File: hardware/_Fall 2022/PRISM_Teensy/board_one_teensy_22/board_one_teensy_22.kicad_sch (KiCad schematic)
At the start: 14 parts, among them J1 EAST, J2 CORE_IO, J3 USB_micro, U1 Teensy4.1, U2 BNO055_Breakout, U3 3966

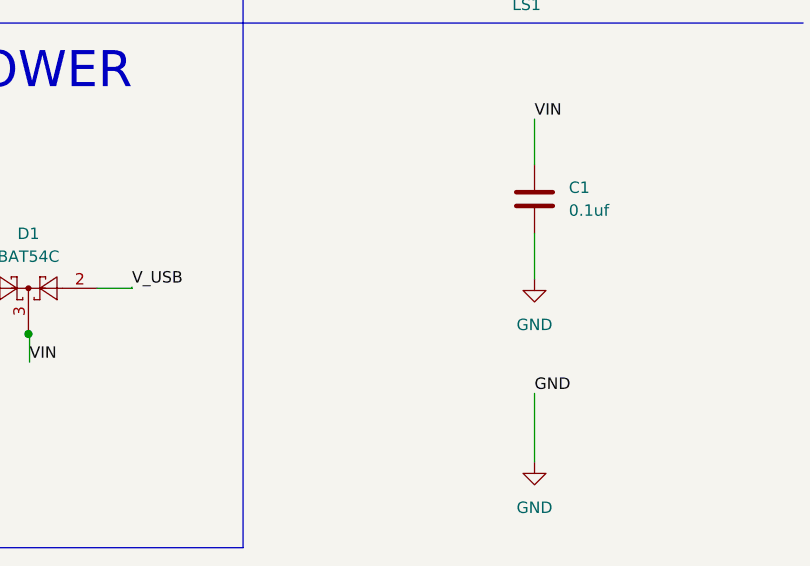
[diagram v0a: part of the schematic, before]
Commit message: Board one changed resistor size
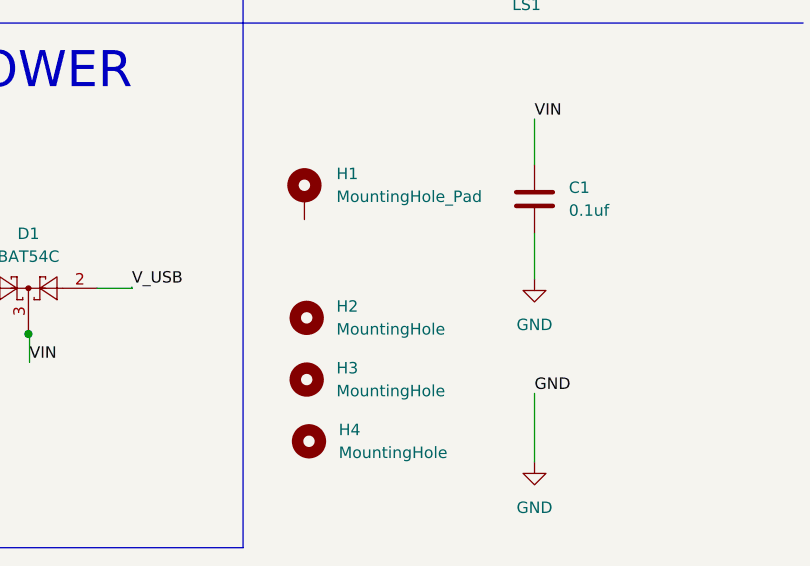
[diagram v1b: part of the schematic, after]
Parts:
- added H1: MountingHole_Pad, MountingHole:MountingHole_3.2mm_M3_DIN965_Pad_TopBottom, symbol Mechanical:MountingHole_Pad
- added H2, H3, H4: MountingHole, MountingHole:MountingHole_3.2mm_M3_DIN965_Pad_TopBottom, symbol Mechanical:MountingHole
- C1, C2: footprint Capacitor_SMD:C_0201_0603Metric -> Capacitor_SMD:C_0603_1608Metric
- R4, R5: footprint Resistor_SMD:R_0201_0603Metric -> Resistor_SMD:R_0603_1608Metric
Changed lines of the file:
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@@
     (pin "7")
+  )
+  (symbol (lib_id "Mechanical:MountingHole_Pad") (at 229.3215 89.9049 0) (unit 1)
+    (in_bom yes) (on_board yes) (fields_autoplaced)
+    (property "Reference" "H1" (id 0) (at 232.8775 87.3648 0)
+      (effects (font (size 1.27 1.27)) (justify left))
+    )
+    (property "Value" "MountingHole_Pad" (id 1) (at 232.8775 89.9048 0)
+      (effects (font (size 1.27 1.27)) (justify left))
+    )
+    (property "Footprint" "MountingHole:MountingHole_3.2mm_M3_DIN965_Pad_TopBottom" (id 2) (at 229.3215 89.9049 0)
+      (effects (font (size 1.27 1.27)) hide)
+    )
+    (property "Datasheet" "~" (id 3) (at 229.3215 89.9049 0)
+      (effects (font (size 1.27 1.27)) hide)
+    )
+    (pin "1")
   )
   (symbol (lib_id "Device:SMT-0827-S-HT-R") (at 254 62.23 90) (unit 1)
@@
     (pin "P")
   )
+  (symbol (lib_id "Mechanical:MountingHole") (at 229.5755 103.3669 0) (unit 1)
+    (in_bom yes) (on_board yes) (fields_autoplaced)
+    (property "Reference" "H2" (id 0) (at 232.8775 102.0968 0)
+      (effects (font (size 1.27 1.27)) (justify left))
+    )
+    (property "Value" "MountingHole" (id 1) (at 232.8775 104.6368 0)
+      (effects (font (size 1.27 1.27)) (justify left))
+    )
+    (property "Footprint" "MountingHole:MountingHole_3.2mm_M3_DIN965_Pad_TopBottom" (id 2) (at 229.5755 103.3669 0)
+      (effects (font (size 1.27 1.27)) hide)
+    )
+    (property "Datasheet" "~" (id 3) (at 229.5755 103.3669 0))
+  )
+  (symbol (lib_id "Mechanical:MountingHole") (at 229.8295 117.0829 0) (unit 1)
+    (in_bom yes) (on_board yes) (fields_autoplaced)
+    (property "Reference" "H4" (id 0) (at 233.1315 115.8128 0)
+      (effects (font (size 1.27 1.27)) (justify left))
+    )
+    (property "Value" "MountingHole" (id 1) (at 233.1315 118.3528 0)
+      (effects (font (size 1.27 1.27)) (justify left))
+    )
+    (property "Footprint" "MountingHole:MountingHole_3.2mm_M3_DIN965_Pad_TopBottom" (id 2) (at 229.8295 117.0829 0)
+      (effects (font (size 1.27 1.27)) hide)
+    )
+    (property "Datasheet" "~" (id 3) (at 229.8295 117.0829 0))
+  )
   (symbol (lib_id "Device:C") (at 243.586 42.164 180) (unit 1)
     (in_bom yes) (on_board yes)
@@
       (effects (font (size 1.27 1.27)) (justify left))
     )
-    (property "Footprint" "Capacitor_SMD:C_0201_0603Metric" (id 2) (at 242.6208 38.354 0)
+    (property "Footprint" "Capacitor_SMD:C_0603_1608Metric" (id 2) (at 242.6208 38.354 0)
       (effects (font (size 1.27 1.27)) hide)
     )
@@
     (pin "1")
   )
+  (symbol (lib_id "Mechanical:MountingHole") (at 229.5755 110.2249 0) (unit 1)
+    (in_bom yes) (on_board yes) (fields_autoplaced)
+    (property "Reference" "H3" (id 0) (at 232.8775 108.9548 0)
+      (effects (font (size 1.27 1.27)) (justify left))
+    )
+    (property "Value" "MountingHole" (id 1) (at 232.8775 111.4948 0)
+      (effects (font (size 1.27 1.27)) (justify left))
+    )
+    (property "Footprint" "MountingHole:MountingHole_3.2mm_M3_DIN965_Pad_TopBottom" (id 2) (at 229.5755 110.2249 0)
+      (effects (font (size 1.27 1.27)) hide)
+    )
+    (property "Datasheet" "~" (id 3) (at 229.5755 110.2249 0))
+  )
   (symbol (lib_id "Device:R") (at 109.855 40.005 0) (unit 1)
     (in_bom yes) (on_board yes) (fields_autoplaced)
@@
       (effects (font (size 1.27 1.27)) (justify left))
     )
-    (property "Footprint" "Resistor_SMD:R_0201_0603Metric" (id 2) (at 108.077 40.005 90)
+    (property "Footprint" "Resistor_SMD:R_0603_1608Metric" (id 2) (at 108.077 40.005 90)
       (effects (font (size 1.27 1.27)) hide)
     )
@@
       (effects (font (size 1.27 1.27)) (justify left))
     )
-    (property "Footprint" "Resistor_SMD:R_0201_0603Metric" (id 2) (at 108.077 50.165 90)
+    (property "Footprint" "Resistor_SMD:R_0603_1608Metric" (id 2) (at 108.077 50.165 90)
       (effects (font (size 1.27 1.27)) hide)
     )
@@
       (effects (font (size 1.27 1.27)) (justify left))
     )
-    (property "Footprint" "Capacitor_SMD:C_0201_0603Metric" (id 2) (at 255.8542 93.98 0)
+    (property "Footprint" "Capacitor_SMD:C_0603_1608Metric" (id 2) (at 255.8542 93.98 0)
       (effects (font (size 1.27 1.27)) hide)
     )
@@
     )
     (path "/ed2d98ad-ef42-4a14-aff6-3752d42a2ad5"
-      (reference "C1") (unit 1) (value "0.1uf") (footprint "Capacitor_SMD:C_0201_0603Metric")
+      (reference "C1") (unit 1) (value "0.1uf") (footprint "Capacitor_SMD:C_0603_1608Metric")
     )
     (path "/8ed0ca95-1fef-48eb-87fb-7d2d377cf6d8"
-      (reference "C2") (unit 1) (value "0.1uf") (footprint "Capacitor_SMD:C_0201_0603Metric")
+      (reference "C2") (unit 1) (value "0.1uf") (footprint "Capacitor_SMD:C_0603_1608Metric")
     )
     (path "/584fd14d-2b31-477f-8140-fcd6e0991dda"
@@
       (reference "D5") (unit 1) (value "Neopixel2") (footprint "neopixel:LED_1655")
     )
+    (path "/635196a9-0bf5-4cbd-add4-521ce790d831"
+      (reference "H1") (unit 1) (value "MountingHole_Pad") (footprint "MountingHole:MountingHole_3.2mm_M3_DIN965_Pad_TopBottom")
+    )
+    (path "/73bf3bdd-f2f8-41cb-97a6-6360d71957c7"
+      (reference "H2") (unit 1) (value "MountingHole") (footprint "MountingHole:MountingHole_3.2mm_M3_DIN965_Pad_TopBottom")
+    )
+    (path "/9503e931-5353-4228-a539-437be4b29a10"
+      (reference "H3") (unit 1) (value "MountingHole") (footprint "MountingHole:MountingHole_3.2mm_M3_DIN965_Pad_TopBottom")
+    )
+    (path "/81f236a2-33a6-4418-bddb-b86279e07556"
+      (reference "H4") (unit 1) (value "MountingHole") (footprint "MountingHole:MountingHole_3.2mm_M3_DIN965_Pad_TopBottom")
+    )
     (path "/c1ad9257-9aae-4dda-b1f1-b68d34349218"
       (reference "J1") (unit 1) (value "EAST") (footprint "Connector_JST:JST_PH_S4B-PH-K_1x04_P2.00mm_Horizontal")
@@
     )
     (path "/99baa0dd-fde4-4b75-83f6-a1af8f8c4b2c"
-      (reference "R4") (unit 1) (value "200K") (footprint "Resistor_SMD:R_0201_0603Metric")
+      (reference "R4") (unit 1) (value "200K") (footprint "Resistor_SMD:R_0603_1608Metric")
     )
     (path "/b35b9880-c31b-4cfc-ab23-116f0c0cec40"
-      (reference "R5") (unit 1) (value "300K") (footprint "Resistor_SMD:R_0201_0603Metric")
+      (reference "R5") (unit 1) (value "300K") (footprint "Resistor_SMD:R_0603_1608Metric")
     )
     (path "/fefe5b14-c21f-486c-b97d-175c68b72866"

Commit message: minor fixes
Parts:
- C1, C2: JLC C307380 -> (none); Vendor (none) -> C14663
- D1: JLC C369922 -> (none); Vendor (none) -> C369922
- R4: JLC C163495 -> (none); Vendor (none) -> C25811
- R5: JLC C473494 -> (none); Vendor (none) -> C23024
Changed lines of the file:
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@@
       (effects (font (size 1.27 1.27)) hide)
     )
-    (property "JLC" "C369922" (id 4) (at 198.6567 100.081 0)
+    (property "Vendor" "C369922" (id 4) (at 198.6567 100.081 0)
       (effects (font (size 1.27 1.27)) hide)
     )
@@
       (effects (font (size 1.27 1.27)) hide)
     )
-    (property "JLC" "C307380" (id 4) (at 243.586 42.164 0)
+    (property "Vendor" "C14663" (id 4) (at 243.586 42.164 0)
       (effects (font (size 1.27 1.27)) hide)
     )
@@
       (effects (font (size 1.27 1.27)) hide)
     )
-    (property "JLC" "C163495" (id 4) (at 109.855 40.005 0)
+    (property "Vendor" "C25811" (id 4) (at 109.855 40.005 0)
       (effects (font (size 1.27 1.27)) hide)
     )
@@
       (effects (font (size 1.27 1.27)) hide)
     )
-    (property "JLC" "C473494" (id 4) (at 109.855 50.165 0)
+    (property "Vendor" "C23024" (id 4) (at 109.855 50.165 0)
       (effects (font (size 1.27 1.27)) hide)
     )
@@
       (effects (font (size 1.27 1.27)) hide)
     )
-    (property "JLC" "C307380" (id 4) (at 254.889 90.17 0)
-      (effects (font (size 1.27 1.27)) hide)
-    )
+    (property "Vendor" "C14663" (id 4) (at 254.889 90.17 0)
+      (effects (font (size 1.27 1.27)) hide)
+    )

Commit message: Board one complete
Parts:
- removed D1: BAT54C, Package_TO_SOT_SMD:SOT-23, symbol Diode:BAT54C
- added D1, D2: SS54, JLC_footprints:DO-214AC, symbol SS54:SS54
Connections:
- net VIN: now also D1.C, D2.C
- net V_BATT: now also D1.A
- net V_USB: now also D2.A
- net CS: no longer names the net of U1.12 (10_CS_MQSR)
- no-connect marks 60 -> 61
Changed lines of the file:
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@@
   (junction (at 109.855 34.925) (diameter 0) (color 0 0 0 0)
   )
-  (junction (at 191.0367 100.081) (diameter 0) (color 0 0 0 0)
-  )
   (junction (at 243.586 46.99) (diameter 0) (color 0 0 0 0)
   )
+  (junction (at 196.6449 104.5757) (diameter 0) (color 0 0 0 0)
+  )
   (junction (at 109.855 45.085) (diameter 0) (color 0 0 0 0)
   )
   (junction (at 254.254 47.117) (diameter 0) (color 0 0 0 0)
   )
+  (junction (at 203.4621 101.0715) (diameter 0) (color 0 0 0 0)
+  )
   (junction (at 243.586 31.877) (diameter 0) (color 0 0 0 0)
-  )
-  (junction (at 198.6567 105.161) (diameter 0) (color 0 0 0 0)
   )
   (no_connect (at 37.465 55.245))
@@
   (no_connect (at 163.068 41.148))
   (no_connect (at 37.465 45.085))
+  (no_connect (at 229.3215 92.4449))
   (no_connect (at 37.465 67.945))
   (no_connect (at 37.465 65.405))
@@
     (stroke (width 0) (type default) (color 0 0 0 0))
   )
-  (wire (pts (xy 206.2767 100.081) (xy 210.1573 100.081))
-    (stroke (width 0) (type default) (color 0 0 0 0))
-  )
   (wire (pts (xy 210.058 55.88) (xy 198.628 55.88))
     (stroke (width 0) (type default) (color 0 0 0 0))
@@
     (stroke (width 0) (type default) (color 0 0 0 0))
   )
-  (wire (pts (xy 198.7821 108.2988) (xy 198.7821 105.161))
-    (stroke (width 0) (type default) (color 0 0 0 0))
-  )
   (wire (pts (xy 210.058 48.26) (xy 198.628 48.26))
     (stroke (width 0) (type default) (color 0 0 0 0))
@@
     (stroke (width 0) (type default) (color 0 0 0 0))
   )
-  (wire (pts (xy 198.7821 105.161) (xy 198.6567 105.161))
-    (stroke (width 0) (type default) (color 0 0 0 0))
-  )
   (wire (pts (xy 198.628 33.02) (xy 198.628 32.766))
     (stroke (width 0) (type default) (color 0 0 0 0))
   )
-  (wire (pts (xy 186.35 100.0946) (xy 191.0367 100.0946))
-    (stroke (width 0) (type default) (color 0 0 0 0))
-  )
   (polyline (pts (xy 12.065 128.905) (xy 125.73 128.905))
     (stroke (width 0) (type default) (color 0 0 0 0))
@@
     (stroke (width 0) (type default) (color 0 0 0 0))
   )
+  (wire (pts (xy 196.6988 104.4906) (xy 196.6449 104.5757))
+    (stroke (width 0) (type default) (color 0 0 0 0))
+  )
   (wire (pts (xy 109.855 34.925) (xy 109.855 36.195))
     (stroke (width 0) (type default) (color 0 0 0 0))
@@
     (stroke (width 0) (type default) (color 0 0 0 0))
   )
+  (wire (pts (xy 196.6449 106.3005) (xy 196.6449 104.5757))
+    (stroke (width 0) (type default) (color 0 0 0 0))
+  )
   (wire (pts (xy 243.586 31.877) (xy 243.586 38.354))
     (stroke (width 0) (type default) (color 0 0 0 0))
   )
+  (wire (pts (xy 207.1209 101.0715) (xy 203.4621 101.0715))
+    (stroke (width 0) (type default) (color 0 0 0 0))
+  )
   (wire (pts (xy 254.889 111.76) (xy 254.889 119.38))
     (stroke (width 0) (type default) (color 0 0 0 0))
@@
     (stroke (width 0) (type default) (color 0 0 0 0))
   )
+  (wire (pts (xy 203.4621 104.5757) (xy 201.7249 104.5757))
+    (stroke (width 0) (type default) (color 0 0 0 0))
+  )
   (wire (pts (xy 109.855 43.815) (xy 109.855 45.085))
     (stroke (width 0) (type default) (color 0 0 0 0))
@@
     (stroke (width 0) (type default) (color 0 0 0 0))
   )
+  (wire (pts (xy 191.9188 98.0826) (xy 191.9188 98.2372))
+    (stroke (width 0) (type default) (color 0 0 0 0))
+  )
   (wire (pts (xy 93.345 55.245) (xy 97.155 55.245))
     (stroke (width 0) (type default) (color 0 0 0 0))
@@
     (stroke (width 0) (type default) (color 0 0 0 0))
   )
+  (wire (pts (xy 203.4621 101.0715) (xy 203.4621 104.5757))
+    (stroke (width 0) (type default) (color 0 0 0 0))
+  )
   (wire (pts (xy 93.345 93.345) (xy 100.2343 93.345))
     (stroke (width 0) (type default) (color 0 0 0 0))
@@
     (stroke (width 0) (type default) (color 0 0 0 0))
   )
-  (wire (pts (xy 24.765 62.865) (xy 37.465 62.865))
+  (wire (pts (xy 196.2326 98.0826) (xy 191.9188 98.0826))
     (stroke (width 0) (type default) (color 0 0 0 0))
   )
@@
     (stroke (width 0) (type default) (color 0 0 0 0))
   )
-  (wire (pts (xy 210.1573 100.081) (xy 210.1573 99.9436))
+  (wire (pts (xy 191.7642 106.3005) (xy 196.6449 106.3005))
     (stroke (width 0) (type default) (color 0 0 0 0))
   )
@@
     (stroke (width 0) (type default) (color 0 0 0 0))
   )
+  (wire (pts (xy 201.3126 98.0826) (xy 203.4621 98.0826))
+    (stroke (width 0) (type default) (color 0 0 0 0))
+  )
   (wire (pts (xy 243.586 45.974) (xy 243.586 46.99))
     (stroke (width 0) (type default) (color 0 0 0 0))
@@
     (stroke (width 0) (type default) (color 0 0 0 0))
   )
+  (wire (pts (xy 203.4621 98.0826) (xy 203.4621 101.0715))
+    (stroke (width 0) (type default) (color 0 0 0 0))
+  )
   (wire (pts (xy 279.4 66.04) (xy 259.08 66.04))
-    (stroke (width 0) (type default) (color 0 0 0 0))
-  )
-  (wire (pts (xy 191.0367 100.0946) (xy 191.0367 100.081))
     (stroke (width 0) (type default) (color 0 0 0 0))
   )
@@
     (effects (font (size 1.27 1.27)) (justify right bottom))
   )
-  (label "VIN" (at 198.7821 108.2988 0)
-    (effects (font (size 1.27 1.27)) (justify left bottom))
-  )
   (label "GND" (at 210.058 60.96 180)
     (effects (font (size 1.27 1.27)) (justify right bottom))
   )
+  (label "V_BATT" (at 191.9188 98.2372 180)
+    (effects (font (size 1.27 1.27)) (justify right bottom))
+  )
   (label "BUZZER" (at 234.95 66.04 180)
     (effects (font (size 1.27 1.27)) (justify right bottom))
@@
     (effects (font (size 1.27 1.27)) (justify left bottom))
   )
-  (label "V_USB" (at 210.1573 99.9436 0)
-    (effects (font (size 1.27 1.27)) (justify left bottom))
-  )
   (label "V_USB" (at 28.829 95.885 0)
     (effects (font (size 1.27 1.27)) (justify left bottom))
@@
     (effects (font (size 1.27 1.27)) (justify left bottom))
   )
+  (label "VIN" (at 207.1209 101.0715 0)
+    (effects (font (size 1.27 1.27)) (justify left bottom))
+  )
   (label "CONT 2" (at 210.058 45.72 180)
     (effects (font (size 1.27 1.27)) (justify right bottom))
@@
     (effects (font (size 1.27 1.27)) (justify left bottom))
   )
+  (label "V_USB" (at 191.7642 106.3005 180)
+    (effects (font (size 1.27 1.27)) (justify right bottom))
+  )
   (label "SDA 0" (at 97.155 55.245 0)
     (effects (font (size 1.27 1.27)) (justify left bottom))
@@
     (effects (font (size 1.27 1.27)) (justify left bottom))
   )
-  (label "CS" (at 24.765 62.865 0)
-    (effects (font (size 1.27 1.27)) (justify left bottom))
-  )
   (label "PYRO 2" (at 24.765 75.565 0)
     (effects (font (size 1.27 1.27)) (justify left bottom))
   )
-  (label "V_BATT" (at 186.35 100.0946 180)
-    (effects (font (size 1.27 1.27)) (justify right bottom))
-  )
   (label "GND" (at 24.765 34.925 0)
     (effects (font (size 1.27 1.27)) (justify left bottom))
@@
     (effects (font (size 1.27 1.27)) (justify right bottom))
   )
-  (symbol (lib_id "Diode:BAT54C") (at 198.6567 100.081 0) (unit 1)
-    (in_bom yes) (on_board yes) (fields_autoplaced)
-    (property "Reference" "D1" (id 0) (at 198.6567 94.0197 0))
-    (property "Value" "BAT54C" (id 1) (at 198.6567 96.5597 0))
-    (property "Footprint" "Package_TO_SOT_SMD:SOT-23" (id 2) (at 200.5617 96.906 0)
-      (effects (font (size 1.27 1.27)) (justify left) hide)
-    )
-    (property "Datasheet" "http://www.diodes.com/_files/datasheets/ds11005.pdf" (id 3) (at 196.6247 100.081 0)
-      (effects (font (size 1.27 1.27)) hide)
-    )
-    (property "Vendor" "C369922" (id 4) (at 198.6567 100.081 0)
-      (effects (font (size 1.27 1.27)) hide)
-    )
-    (pin "1")
-    (pin "2")
-    (pin "3")
+  (symbol (lib_id "SS54:SS54") (at 198.7726 98.0826 0) (unit 1)
+    (in_bom yes) (on_board yes)
+    (property "Reference" "D1" (id 0) (at 198.7211 93.96 0))
+    (property "Value" "SS54" (id 1) (at 198.6696 95.9182 0))
+    (property "Footprint" "JLC_footprints:DO-214AC" (id 2) (at 198.7726 98.0826 0)
+      (effects (font (size 1.27 1.27)) (justify bottom) hide)
+    )
+    (property "Datasheet" "" (id 3) (at 198.7726 98.0826 0)
+      (effects (font (size 1.27 1.27)) hide)
+    )
+    (property "Vendor" "C22452" (id 4) (at 198.7726 98.0826 0)
+      (effects (font (size 1.27 1.27)) hide)
+    )
+    (pin "A")
+    (pin "C")
   )
   (symbol (lib_id "LED:NeoPixel_THT") (at 273.304 39.497 0) (unit 1)
@@
     (pin "1")
     (pin "2")
+  )
+  (symbol (lib_id "SS54:SS54") (at 199.1849 104.5757 0) (unit 1)
+    (in_bom yes) (on_board yes)
+    (property "Reference" "D2" (id 0) (at 199.1333 102.2052 0))
+    (property "Value" "SS54" (id 1) (at 199.1849 100.7623 0))
+    (property "Footprint" "JLC_footprints:DO-214AC" (id 2) (at 199.1849 104.5757 0)
+      (effects (font (size 1.27 1.27)) (justify bottom) hide)
+    )
+    (property "Datasheet" "" (id 3) (at 199.1849 104.5757 0)
+      (effects (font (size 1.27 1.27)) hide)
+    )
+    (property "Vendor" "C22452" (id 4) (at 199.1849 104.5757 0)
+      (effects (font (size 1.27 1.27)) hide)
+    )
+    (pin "A")
+    (pin "C")
   )
   (symbol (lib_id "REV2_SPRING_2022-rescue:BNO055_Breakout-Sensors_2021_2022") (at 154.178 46.228 0) (unit 1)
@@
       (reference "C2") (unit 1) (value "0.1uf") (footprint "Capacitor_SMD:C_0603_1608Metric")
     )
-    (path "/584fd14d-2b31-477f-8140-fcd6e0991dda"
-      (reference "D1") (unit 1) (value "BAT54C") (footprint "Package_TO_SOT_SMD:SOT-23")
+    (path "/0ef74022-fb23-49b6-87ea-ea00f9a26307"
+      (reference "D1") (unit 1) (value "SS54") (footprint "JLC_footprints:DO-214AC")
+    )
+    (path "/eef0ba06-6612-4d1f-a59c-96c94a80a647"
+      (reference "D2") (unit 1) (value "SS54") (footprint "JLC_footprints:DO-214AC")
     )
     (path "/a2dee755-f29c-470f-8c5e-e23ef91a94a4"

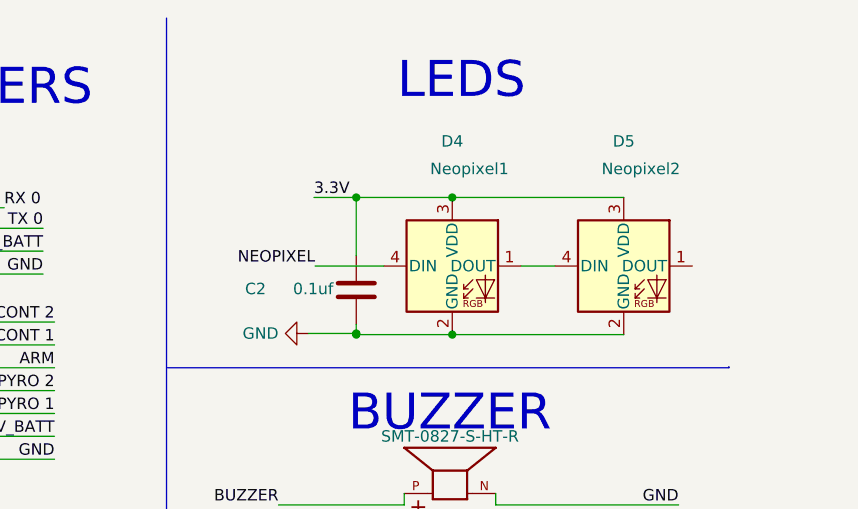
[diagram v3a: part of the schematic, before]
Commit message: Changed neopixel footprint
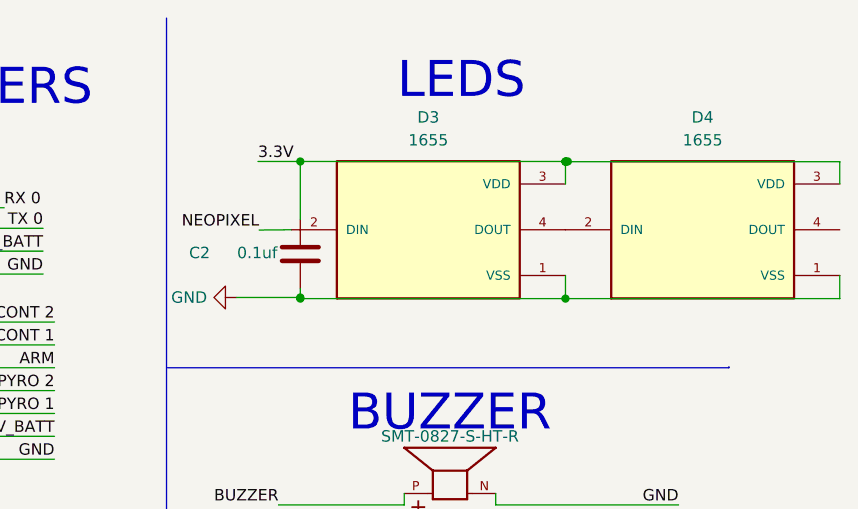
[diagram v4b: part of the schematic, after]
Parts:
- removed D4: Neopixel1, neopixel:LED_1655, symbol LED:NeoPixel_THT
- removed D5: Neopixel2, neopixel:LED_1655, symbol LED:NeoPixel_THT
- added D3, D4: 1655, LED_1655, symbol neopixel:1655
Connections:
- net 3.3V: now also D3.3 (VDD), D4.3 (VDD)
- net GND: now also D3.1 (VSS), D4.1 (VSS)
- net NEOPIXEL: now also D3.2 (DIN)
- new net: D3.4 (DOUT), D4.2 (DIN)
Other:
- moved on the sheet: C2
